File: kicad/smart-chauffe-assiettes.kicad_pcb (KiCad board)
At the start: 2 copper layers, 63.5 x 48.3 mm, 16 parts, among them J1 Conn_01x08_Socket, U1 PIC10F202-IP

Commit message: First attempt at laying out the components
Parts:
- removed R0: 10k, Resistor_THT:R_Axial_DIN0207_L6.3mm_D2.5mm_P2.54mm_Vertical
- removed R10, R9: 100, Resistor_THT:R_Axial_DIN0207_L6.3mm_D2.5mm_P2.54mm_Vertical
- removed U1: PIC10F202-IP, Package_DIP:DIP-8_W7.62mm
- added J2: Conn_01x02_Socket, TerminalBlock_Phoenix:TerminalBlock_Phoenix_MKDS-1,5-2-5.08_1x02_P5.08mm_Horizontal, F.Cu at (101.6, 78.7)
- added J3: Conn_01x02_Socket, TerminalBlock_Phoenix:TerminalBlock_Phoenix_MKDS-1,5-2-5.08_1x02_P5.08mm_Horizontal, F.Cu at (142.2, 78.7)
- added J4: Conn_01x03_Socket, TerminalBlock_Phoenix:TerminalBlock_Phoenix_MKDS-1,5-3-5.08_1x03_P5.08mm_Horizontal, F.Cu at (157.7, 86.4)
- added J5: Conn_01x03_Socket, Connector_PinSocket_2.54mm:PinSocket_1x03_P2.54mm_Vertical, F.Cu at (132.1, 111.8)
- added J6: Conn_01x03_Socket, Connector_PinSocket_2.54mm:PinSocket_1x03_P2.54mm_Vertical, F.Cu at (132.1, 104.1)
- added Q1: 2N3904, Package_TO_SOT_THT:TO-92_Inline_Wide, F.Cu at (139.7, 91.4)
- added R1: 2k, Resistor_THT:R_Axial_DIN0207_L6.3mm_D2.5mm_P2.54mm_Vertical, F.Cu at (142.2, 119.4)
- added R2: 10k, Resistor_THT:R_Axial_DIN0207_L6.3mm_D2.5mm_P2.54mm_Vertical, F.Cu at (129.5, 119.4)
- R3, R6: value 10k -> 220
- R7: value 100 -> 1k
- R8: value 100 -> 10k
- moved R4 126.3 mm to (157.5, 96.5)
- moved R8 124.1 mm to (152.4, 91.4), turned to 180 degrees
- moved R5 118.9 mm to (149.9, 96.5), turned to 180 degrees
- moved R3 117.4 mm to (147.3, 116.8)
- moved J1 117.2 mm to (154.9, 119.4), turned to 180 degrees
- moved R6 116.2 mm to (147.3, 104.1)
- moved R7 112.4 mm to (142.2, 96.5), turned to 180 degrees
- moved C1 97.9 mm to (147.3, 110.3), turned to -90 degrees
- moved C2 88.9 mm to (142.2, 106.7), turned to -90 degrees
- moved RV1 84.3 mm to (131.5, 86.4), turned to -90 degrees
- moved F1 78.5 mm to (112.9, 78.7)
- moved PS1 18.1 mm to (114.2, 88.9), turned to -90 degrees
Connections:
- C1 pad 1: VCC -> SW_SPST_NO_VOUT
- C1 pad 2: GND -> COMMON_GND
- C2 pad 1: VCC -> SW_SPST_NO_VOUT
- C2 pad 2: GND -> COMMON_GND
- J1 pad 1: +3.3V -> LED_ON_TO_GND
- J1 pad 2: VCC -> LED_HEAT_TO_GND
- J1 pad 3: HX711_DATA -> GP2
- J1 pad 4: HX711_CLK -> COMMON_GND
- J1 pad 5: unconnected-(J1-Pin_5-Pad5) -> BUTTON_NO_TO_GND
- J1 pad 6: LED_ACTIVE_TO_GND -> HX711_CLK
- J1 pad 7: BUTTON_NO_TO_GND -> SW_SPST_NO_VIN
- J1 pad 8: GND -> SW_SPST_NO_VOUT
- PS1 pad 3: GND -> COMMON_GND
- PS1 pad 4: +3.3V -> SW_SPST_NO_VIN
- R3 pad 1: Net-(R10-Pad2) -> GP0
- R3 pad 2: LED_ACTIVE_TO_GND -> LED_HEAT_TO_GND
- R4 pad 1: VCC -> SW_SPST_NO_VOUT
- R5 pad 1: VCC -> SW_SPST_NO_VOUT
- R5 pad 2: HX711_DATA -> GP2
- R6 pad 1: HX711_CLK -> GP1
- R6 pad 2: VCC -> HX711_CLK
- R7 pad 1: HX711_DATA -> Net-(Q1-B)
- R7 pad 2: Net-(U1-GP0) -> LED_HEAT_TO_GND
- R8 pad 1: Net-(U1-GP1) -> SW_SPST_NO_VOUT
- R8 pad 2: HX711_CLK -> RELAY_IN_INVERTED

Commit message: First stab at routing
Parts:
- moved R6 7.62 mm to (147.3, 111.8)
- moved C1 6.63 mm to (149.9, 104.1)
- moved J2 5.08 mm to (106.7, 78.7), turned to 180 degrees
- moved R1 5.08 mm to (147.3, 119.4)
- moved R3 5.08 mm to (142.2, 116.8), turned to 90 degrees
- moved Q1 3.59 mm to (142.2, 94.0)
- moved R7 3.59 mm to (144.8, 99.1)
- moved J3 3.59 mm to (144.8, 76.2), turned to -90 degrees
- moved R5 2.54 mm to (152.4, 96.5)
- moved R8 2.54 mm to (154.9, 91.4)
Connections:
- net LINE renamed PHASE
- net NEUT renamed NEUTRAL
- net Net-(PS1-AC/L) renamed FUSED
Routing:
- net COMMON_GND: track 0.00 -> 86.5 mm, vias 0 -> 2
- net SW_SPST_NO_VIN: track 0.00 -> 68.3 mm
- net SW_SPST_NO_VOUT: track 0.00 -> 59.3 mm
- net BUTTON_NO_TO_GND: track 0.00 -> 58.2 mm
- net NEUTRAL: track 0.00 -> 43.9 mm
- net GP2: track 0.00 -> 40.8 mm
- net FUSED: track 0.00 -> 34.6 mm
- net LED_HEAT_TO_GND: track 0.00 -> 31.1 mm
- net RELAY_IN_INVERTED: track 0.00 -> 18.5 mm
- net PHASE: track 0.00 -> 17.8 mm
- net GP0: track 0.00 -> 12.3 mm
- net GP1: track 0.00 -> 10.2 mm
- net LED_ON_TO_GND: track 0.00 -> 7.62 mm
- net HX711_CLK: track 0.00 -> 7.18 mm
- net Net-(Q1-B): track 0.00 -> 5.08 mm

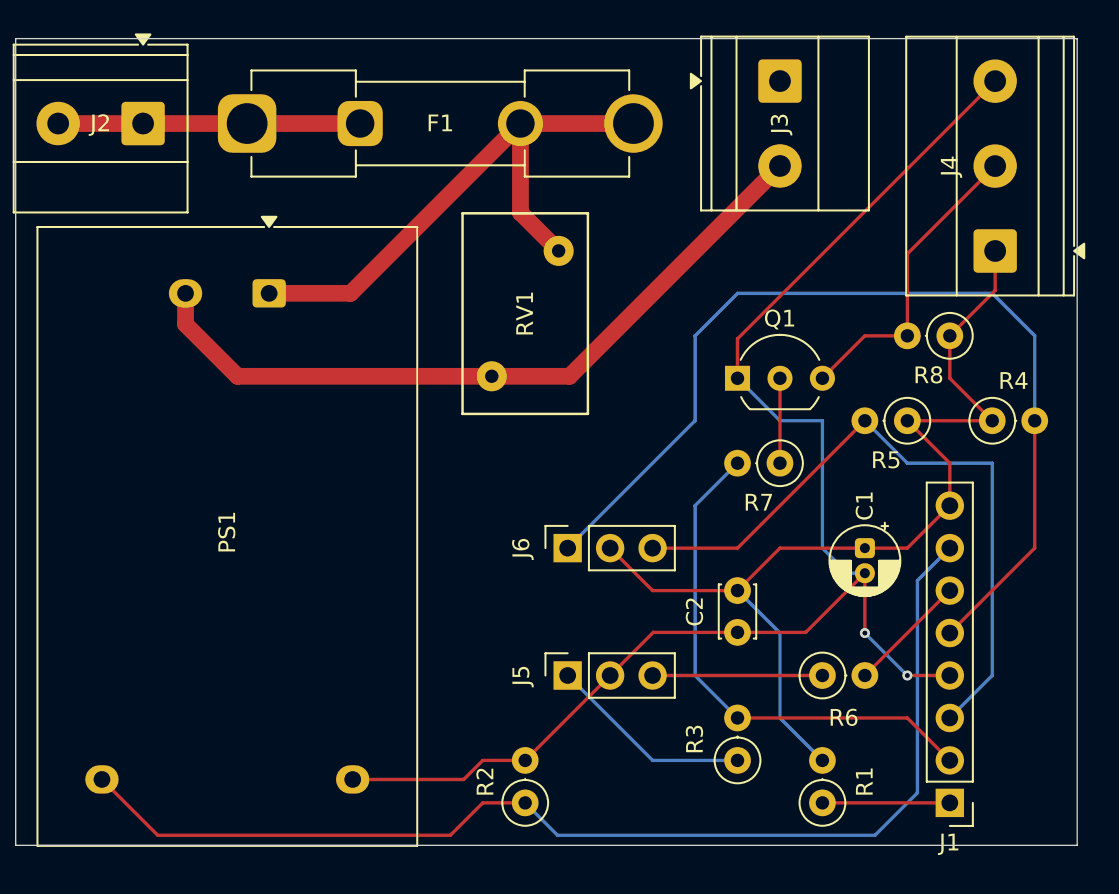
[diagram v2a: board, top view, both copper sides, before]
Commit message: Fix missing power trace and swap psu leads
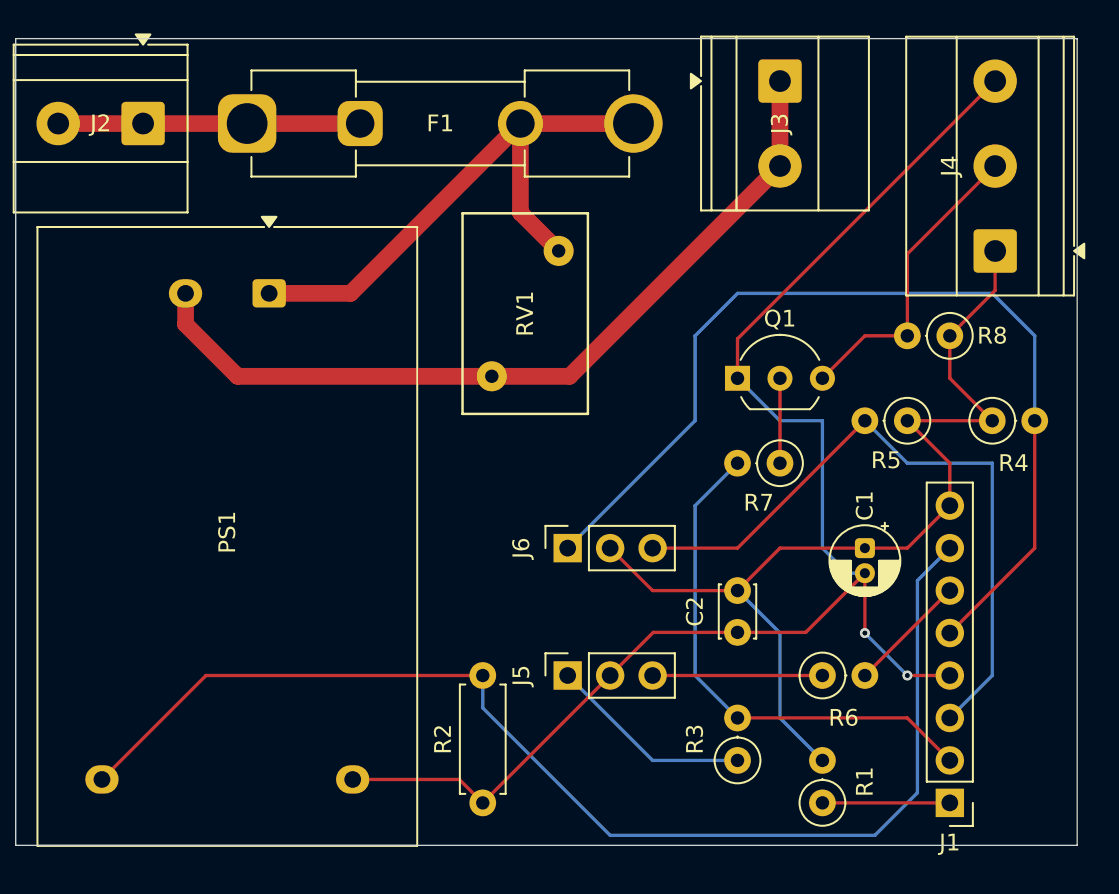
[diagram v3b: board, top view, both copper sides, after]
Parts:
- R2: footprint Resistor_THT:R_Axial_DIN0207_L6.3mm_D2.5mm_P2.54mm_Vertical -> Resistor_THT:R_Axial_DIN0207_L6.3mm_D2.5mm_P7.62mm_Horizontal
- moved R2 2.54 mm to (127.0, 119.4)
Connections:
- R2 pad 1: SW_SPST_NO_VIN -> COMMON_GND
- R2 pad 2: COMMON_GND -> SW_SPST_NO_VIN
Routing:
- net NEUTRAL: track 43.9 -> 49.0 mm
- net SW_SPST_NO_VIN: track 68.3 -> 72.9 mm
- net COMMON_GND: track 86.5 -> 87.7 mm
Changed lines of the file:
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@@
 		)
 	)
-	(footprint "Resistor_THT:R_Axial_DIN0207_L6.3mm_D2.5mm_P2.54mm_Vertical"
+	(footprint "Resistor_THT:R_Axial_DIN0207_L6.3mm_D2.5mm_P7.62mm_Horizontal"
 		(layer "F.Cu")
-		(at 129.54 119.38 90)
-		(descr "Resistor, Axial_DIN0207 series, Axial, Vertical, pin pitch=2.54mm, 0.25W = 1/4W, length*diameter=6.3*2.5mm^2, http://cdn-reichelt.de/documents/datenblatt/B400/1_4W%23YAG.pdf")
-		(tags "Resistor Axial_DIN0207 series Axial Vertical pin pitch 2.54mm 0.25W = 1/4W length 6.3mm diameter 2.5mm")
+		(at 127 119.38 90)
+		(descr "Resistor, Axial_DIN0207 series, Axial, Horizontal, pin pitch=7.62mm, 0.25W = 1/4W, length*diameter=6.3*2.5mm^2, http://cdn-reichelt.de/documents/datenblatt/B400/1_4W%23YAG.pdf")
+		(tags "Resistor Axial_DIN0207 series Axial Horizontal pin pitch 7.62mm 0.25W = 1/4W length 6.3mm diameter 2.5mm")
 		(property "Reference" "R2"
-			(at 1.27 -2.37 90)
+			(at 3.81 -2.37 90)
 			(layer "F.SilkS")
 			(effects
@@
 		)
 		(property "Value" "10k"
-			(at 1.27 2.37 90)
+			(at 3.81 2.37 90)
 			(layer "F.Fab")
 			(effects
@@
 		(attr through_hole)
 		(fp_line
-			(start 1.37 0)
-			(end 1.44 0)
+			(start 7.08 -1.37)
+			(end 7.08 -1.04)
 			(stroke
 				(width 0.12)
@@
 			(layer "F.SilkS")
 		)
-		(fp_circle
-			(center 0 0)
-			(end 1.37 0)
+		(fp_line
+			(start 0.54 -1.37)
+			(end 7.08 -1.37)
+			(stroke
+				(width 0.12)
+				(type solid)
+			)
+			(layer "F.SilkS")
+		)
+		(fp_line
+			(start 0.54 -1.04)
+			(end 0.54 -1.37)
+			(stroke
+				(width 0.12)
+				(type solid)
+			)
+			(layer "F.SilkS")
+		)
+		(fp_line
+			(start 0.54 1.04)
+			(end 0.54 1.37)
+			(stroke
+				(width 0.12)
+				(type solid)
+			)
+			(layer "F.SilkS")
+		)
+		(fp_line
+			(start 7.08 1.37)
+			(end 7.08 1.04)
+			(stroke
+				(width 0.12)
+				(type solid)
+			)
+			(layer "F.SilkS")
+		)
+		(fp_line
+			(start 0.54 1.37)
+			(end 7.08 1.37)
 			(stroke
 				(width 0.12)
 				(type solid)
 			)
-			(fill no)
 			(layer "F.SilkS")
 		)
 		(fp_rect
-			(start -1.5 -1.5)
-			(end 3.59 1.5)
+			(start -1.05 -1.5)
+			(end 8.67 1.5)
 			(stroke
 				(width 0.05)
@@
 		)
 		(fp_line
+			(start 7.62 0)
+			(end 6.96 0)
+			(stroke
+				(width 0.1)
+				(type solid)
+			)
+			(layer "F.Fab")
+		)
+		(fp_line
 			(start 0 0)
-			(end 2.54 0)
+			(end 0.66 0)
 			(stroke
 				(width 0.1)
@@
 			(layer "F.Fab")
 		)
-		(fp_circle
-			(center 0 0)
-			(end 1.25 0)
+		(fp_rect
+			(start 0.66 -1.25)
+			(end 6.96 1.25)
 			(stroke
 				(width 0.1)
@@
 		)
 		(fp_text user "${REFERENCE}"
-			(at 1.27 -2.37 90)
+			(at 3.81 0 90)
 			(layer "F.Fab")
 			(effects
@@
 			(layers "*.Cu" "*.Mask")
 			(remove_unused_layers no)
-			(net 5 "SW_SPST_NO_VIN")
+			(net 2 "COMMON_GND")
 			(pintype "passive")
 		)
 		(pad "2" thru_hole circle
-			(at 2.54 0 90)
+			(at 7.62 0 90)
 			(size 1.6 1.6)
 			(drill 0.8)
 			(layers "*.Cu" "*.Mask")
 			(remove_unused_layers no)
-			(net 2 "COMMON_GND")
+			(net 5 "SW_SPST_NO_VIN")
 			(pintype "passive")
 		)
 		(embedded_fonts no)
-		(model "${KICAD9_3DMODEL_DIR}/Resistor_THT.3dshapes/R_Axial_DIN0207_L6.3mm_D2.5mm_P2.54mm_Vertical.step"
+		(model "${KICAD9_3DMODEL_DIR}/Resistor_THT.3dshapes/R_Axial_DIN0207_L6.3mm_D2.5mm_P7.62mm_Horizontal.step"
 			(offset
 				(xyz 0 0 0)
@@
 		(tags "Resistor Axial_DIN0207 series Axial Vertical pin pitch 2.54mm 0.25W = 1/4W length 6.3mm diameter 2.5mm")
 		(property "Reference" "R8"
-			(at 1.27 -2.37 0)
+			(at -2.54 0 0)
 			(layer "F.SilkS")
 			(effects
@@
 		(tags "Resistor Axial_DIN0207 series Axial Vertical pin pitch 2.54mm 0.25W = 1/4W length 6.3mm diameter 2.5mm")
 		(property "Reference" "R4"
-			(at 1.27 -2.37 0)
+			(at 1.27 2.54 0)
 			(layer "F.SilkS")
 			(effects
@@
 	)
 	(segment
-		(start 129.54 116.84)
-		(end 127 116.84)
+		(start 119.22 117.98)
+		(end 125.6 117.98)
 		(width 0.2)
 		(layer "F.Cu")
@@
 	)
 	(segment
-		(start 125.86 117.98)
-		(end 119.22 117.98)
-		(width 0.2)
-		(layer "F.Cu")
-		(net 2)
-	)
-	(segment
 		(start 149.86 105.64)
 		(end 149.86 109.22)
@@
 	)
 	(segment
-		(start 129.54 116.84)
-		(end 134.62 111.76)
-		(width 0.2)
-		(layer "F.Cu")
-		(net 2)
-	)
-	(segment
 		(start 137.2 109.18)
 		(end 142.24 109.18)
@@
 	)
 	(segment
-		(start 127 116.84)
-		(end 125.86 117.98)
+		(start 127 119.38)
+		(end 134.62 111.76)
 		(width 0.2)
 		(layer "F.Cu")
@@
 	)
 	(segment
+		(start 125.6 117.98)
+		(end 127 119.38)
+		(width 0.2)
+		(layer "F.Cu")
+		(net 2)
+	)
+	(segment
 		(start 152.4 111.76)
 		(end 154.94 111.76)
@@
 	)
 	(segment
-		(start 127 119.38)
-		(end 125.061 121.319)
+		(start 110.44 111.76)
+		(end 127 111.76)
 		(width 0.2)
 		(layer "F.Cu")
@@
 	)
 	(segment
-		(start 107.559 121.319)
-		(end 104.22 117.98)
+		(start 104.22 117.98)
+		(end 110.44 111.76)
 		(width 0.2)
 		(layer "F.Cu")
@@
 	)
 	(segment
-		(start 125.061 121.319)
-		(end 107.559 121.319)
+		(start 127 111.76)
+		(end 127 113.699)
 		(width 0.2)
-		(layer "F.Cu")
+		(layer "B.Cu")
 		(net 5)
 	)
 	(segment
-		(start 129.54 119.38)
-		(end 127 119.38)
+		(start 154.94 104.14)
+		(end 153.001 106.079)
 		(width 0.2)
-		(layer "F.Cu")
+		(layer "B.Cu")
 		(net 5)
 	)
 	(segment
-		(start 154.94 104.14)
-		(end 153.001 106.079)
+		(start 134.62 121.319)
+		(end 150.461 121.319)
 		(width 0.2)
 		(layer "B.Cu")
@@
 	)
 	(segment
-		(start 150.461 121.319)
-		(end 131.479 121.319)
+		(start 127 113.699)
+		(end 134.62 121.319)
 		(width 0.2)
 		(layer "B.Cu")
@@
 	)
 	(segment
-		(start 131.479 121.319)
-		(end 129.54 119.38)
-		(width 0.2)
-		(layer "B.Cu")
-		(net 5)
-	)
-	(segment
 		(start 147.32 119.38)
 		(end 154.94 119.38)
@@
 		(width 1)
 		(layer "F.Cu")
+		(net 11)
+	)
+	(segment
+		(start 144.78 76.2)
+		(end 144.78 81.28)
+		(width 1)
+		(layer "F.Cu")
